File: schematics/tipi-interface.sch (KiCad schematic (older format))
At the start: 18 parts

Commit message: Update for control signalling.
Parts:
- removed R3, R?: 1k, symbol R
- removed U? (x3): 74LS21, symbol 74LS21
- removed U? (x3): 74HC04, symbol 74HC04
- removed U?: 74LS20, symbol 74LS20
- added R?: 1k, symbol R
- added U?: 74LS373, symbol 74LS373
- added U?: 74LVC245, symbol 74LVC245
- added U?: 74LS138, symbol 74LS138
- added U? (x3): 74HC04, symbol 74HC04
- added U?: 74LS21, symbol 74LS21
- added U?: 74HC245, symbol 74HC245
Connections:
- net labels removed: +5V
- wire segments 146 -> 192
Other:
- moved on the sheet: R1, U?, U?A, U?B

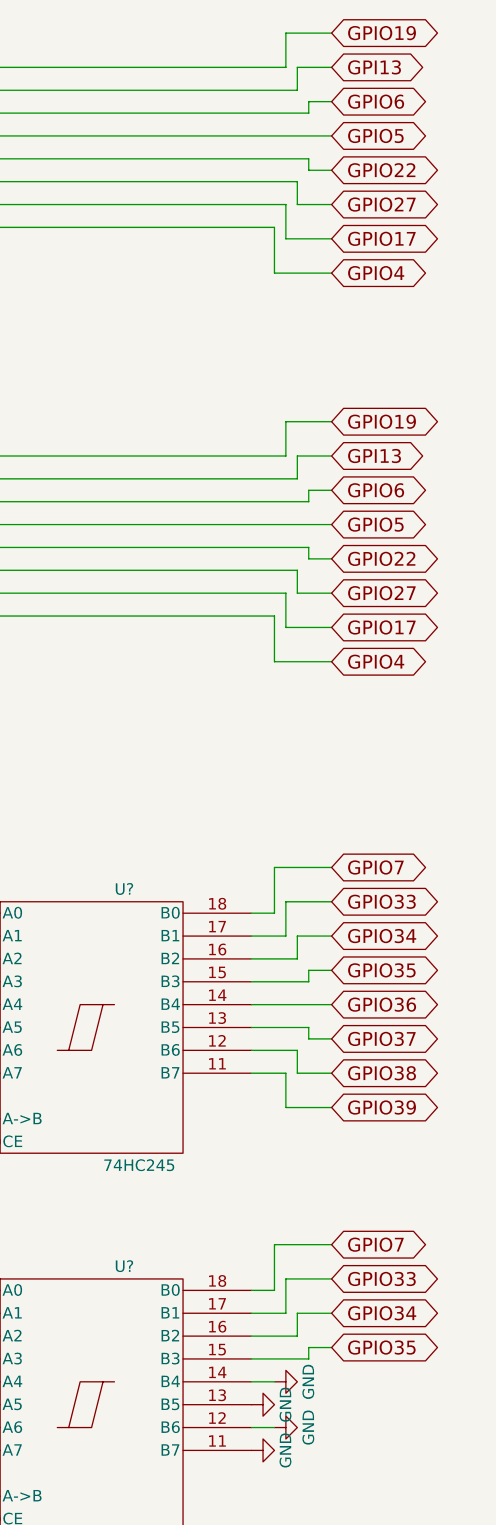
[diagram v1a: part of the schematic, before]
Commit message: Set appropriate RPi GPIO pin assignments.
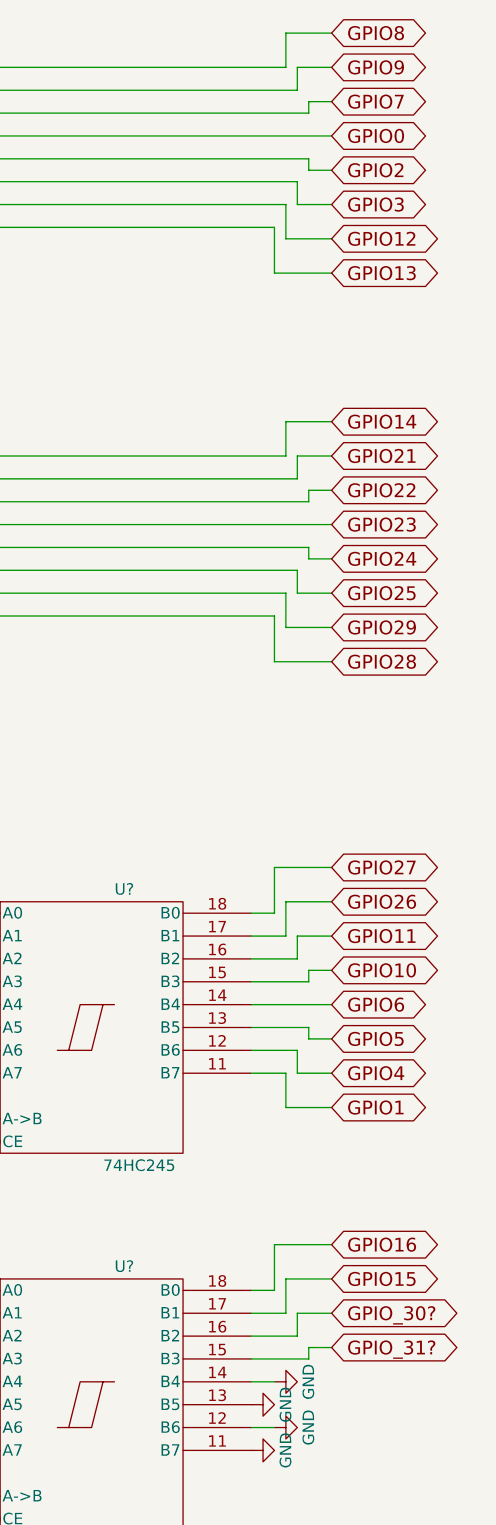
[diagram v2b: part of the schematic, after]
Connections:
- net GPIO36 is gone; now on net GPIO6: U?.14 (B4)
- net GPIO37 is gone; now on net GPIO5: U?.13 (B5)
- net GPIO38 is gone; now on net GPIO4: U?.12 (B6)
- net GPIO22: now also U?.16 (B2); no longer U?.14 (B4), U?.14 (B4)
- net GPIO27: now also U?.18 (B0); no longer U?.13 (B5), U?.13 (B5)
- net GPIO4: no longer U?.11 (B7), U?.11 (B7)
- net GPIO5: no longer U?.15 (B3), U?.15 (B3)
- net GPIO6: no longer U?.16 (B2), U?.16 (B2)
- net GPIO7: now also U?.16 (B2); no longer U?.18 (B0), U?.18 (B0)
- net GPI13 renamed GPIO21
- net GPIO21: no longer U?.17 (B1)
- net GPIO17 renamed GPIO12
- net GPIO12: no longer U?.12 (B6)
- net GPIO19 renamed GPIO14
- net GPIO14: no longer U?.18 (B0)
- net GPIO33 renamed GPIO15
- net GPIO15: no longer U?.17 (B1)
- net GPIO34 renamed GPIO11
- net GPIO11: no longer U?.16 (B2)
- net GPIO35 renamed GPIO10
- net GPIO10: no longer U?.15 (B3)
- net GPIO39 renamed GPIO1
- new net GPIO0: U?.15 (B3)
- new net GPIO13: U?.11 (B7)
- new net GPIO16: U?.18 (B0)
- new net GPIO2: U?.14 (B4)
- new net GPIO23: U?.15 (B3)
- new net GPIO24: U?.14 (B4)
- new net GPIO25: U?.13 (B5)
- new net GPIO26: U?.17 (B1)
- new net GPIO28: U?.11 (B7)
- new net GPIO29: U?.12 (B6)
- new net GPIO3: U?.13 (B5)
- new net GPIO8: U?.18 (B0)
- new net GPIO9: U?.17 (B1)
- new net GPIO_30?: U?.16 (B2)
- new net GPIO_31?: U?.15 (B3)
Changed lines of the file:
@@
 $EndComp
 Text GLabel 10050 3150 2    60   BiDi ~ 0
-GPIO19
+GPIO14
 Text GLabel 10050 3300 2    60   BiDi ~ 0
-GPI13
+GPIO21
 Text GLabel 10050 3450 2    60   BiDi ~ 0
-GPIO6
+GPIO22
 Text GLabel 10050 3600 2    60   BiDi ~ 0
-GPIO5
+GPIO23
 Text GLabel 10050 3750 2    60   BiDi ~ 0
-GPIO22
+GPIO24
 Text GLabel 10050 3900 2    60   BiDi ~ 0
-GPIO27
+GPIO25
 Text GLabel 10050 4050 2    60   BiDi ~ 0
-GPIO17
+GPIO29
 Text GLabel 10050 4200 2    60   BiDi ~ 0
-GPIO4
+GPIO28
 $Comp
 L 74LS373 U?
@@
 $EndComp
 Text GLabel 10050 5100 2    60   BiDi ~ 0
-GPIO7
+GPIO27
 Text GLabel 10050 5250 2    60   BiDi ~ 0
-GPIO33
+GPIO26
 Text GLabel 10050 5400 2    60   BiDi ~ 0
-GPIO34
+GPIO11
 Text GLabel 10050 5550 2    60   BiDi ~ 0
-GPIO35
+GPIO10
 Text GLabel 10050 5700 2    60   BiDi ~ 0
-GPIO36
+GPIO6
 Text GLabel 10050 5850 2    60   BiDi ~ 0
-GPIO37
+GPIO5
 Text GLabel 10050 6000 2    60   BiDi ~ 0
-GPIO38
+GPIO4
 Text GLabel 10050 6150 2    60   BiDi ~ 0
-GPIO39
+GPIO1
 Entry Wire Line
 	8200 5200 8300 5300
@@
 $EndComp
 Text GLabel 10050 1450 2    60   BiDi ~ 0
-GPIO19
+GPIO8
 Text GLabel 10050 1600 2    60   BiDi ~ 0
-GPI13
+GPIO9
 Text GLabel 10050 1750 2    60   BiDi ~ 0
-GPIO6
+GPIO7
 Text GLabel 10050 1900 2    60   BiDi ~ 0
-GPIO5
+GPIO0
 Text GLabel 10050 2050 2    60   BiDi ~ 0
-GPIO22
+GPIO2
 Text GLabel 10050 2200 2    60   BiDi ~ 0
-GPIO27
+GPIO3
 Text GLabel 10050 2350 2    60   BiDi ~ 0
-GPIO17
+GPIO12
 Text GLabel 10050 2500 2    60   BiDi ~ 0
-GPIO4
+GPIO13
 $Comp
 L 74LS373 U?
@@
 $EndComp
 Text GLabel 10050 6750 2    60   BiDi ~ 0
-GPIO7
+GPIO16
 Text GLabel 10050 6900 2    60   BiDi ~ 0
-GPIO33
+GPIO15
 Text GLabel 10050 7050 2    60   BiDi ~ 0
-GPIO34
+GPIO_30?
 Text GLabel 10050 7200 2    60   BiDi ~ 0
-GPIO35
-$Comp
-L GND #PWR?
+GPIO_31?
+$Comp
+L GND #PWR?

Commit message: Add CRU bit to enable/disable board.
Use a 4 bit jumper header block to select nibble x in the address 1x00h. The bit responds at any and all addresses inclusively between 1x00h and 1xFFh. However the circuit should be programmed to bit offset 0 only. Future bits
will be intendend for bank switch ROM.
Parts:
- added P?: CONN_02X04, symbol CONN_02X04
- added R? (x5): 1k, symbol R
- added U?: 74LS688, symbol 74LS688
- added U?: 74LS74, symbol 74LS74
- added U?: 7402, symbol 7402
- added U?: 74LS08, symbol 74LS08
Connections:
- net labels added: +5V, CRU-BIT1, RESET*
- wire segments 192 -> 234
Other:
- moved on the sheet: R1, R?, U?, U?A, U?B

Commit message: Fix issue with cru addressing off by a bit.
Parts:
- removed P?: CONN_02X04, symbol CONN_02X04
- added R?: 1k, symbol R
- added SW?: Coded_Switch, symbol Coded_Switch
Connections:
- wire segments 234 -> 231
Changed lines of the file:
@@
 Sheet 1 1
 Title "TI Raspberry PI interface"
-Date "2017-01-21"
+Date "2017-01-22"
 Rev "4"
 Comp "ElectricLab & Jedimatt42"
@@
 L GND #PWR?
 U 1 1 5882E6A1
-P 2000 1150
-F 0 "#PWR?" H 2000 900 50  0001 C CNN
-F 1 "GND" H 2000 1000 50  0000 C CNN
-F 2 "" H 2000 1150 50  0000 C CNN
-F 3 "" H 2000 1150 50  0000 C CNN
-	1    2000 1150
+P 2000 1450
+F 0 "#PWR?" H 2000 1200 50  0001 C CNN
+F 1 "GND" H 2000 1300 50  0000 C CNN
+F 2 "" H 2000 1450 50  0000 C CNN
+F 3 "" H 2000 1450 50  0000 C CNN
+	1    2000 1450
 	0    1    1    0
-$EndComp
-$Comp
-L CONN_02X04 P?
-U 1 1 5882E705
-P 1250 1750
-F 0 "P?" H 1250 2000 50  0000 C CNN
-F 1 "CONN_02X04" H 1250 1500 50  0000 C CNN
-F 2 "" H 1250 550 50  0000 C CNN
-F 3 "" H 1250 550 50  0000 C CNN
-	1    1250 1750
-	1    0    0    -1
 $EndComp
 $Comp
@@
 $Comp
 L GND #PWR?
-U 1 1 588304B3
-P 900 1900
-F 0 "#PWR?" H 900 1650 50  0001 C CNN
-F 1 "GND" H 900 1750 50  0000 C CNN
-F 2 "" H 900 1900 50  0000 C CNN
-F 3 "" H 900 1900 50  0000 C CNN
-	1    900  1900
-	1    0    0    -1
-$EndComp
-$Comp
-L GND #PWR?
 U 1 1 5883155D
-P 2050 2000
-F 0 "#PWR?" H 2050 1750 50  0001 C CNN
-F 1 "GND" H 2050 1850 50  0000 C CNN
-F 2 "" H 2050 2000 50  0000 C CNN
-F 3 "" H 2050 2000 50  0000 C CNN
-	1    2050 2000
+P 2050 2300
+F 0 "#PWR?" H 2050 2050 50  0001 C CNN
+F 1 "GND" H 2050 2150 50  0000 C CNN
+F 2 "" H 2050 2300 50  0000 C CNN
+F 3 "" H 2050 2300 50  0000 C CNN
+	1    2050 2300
 	0    1    1    0
 $EndComp
@@
 	7650 9100 8250 9100
 Wire Wire Line
-	900  1600 1000 1600
-Wire Wire Line
-	900  1600 900  1900
-Wire Wire Line
-	900  1700 1000 1700
-Wire Wire Line
-	900  1800 1000 1800
-Connection ~ 900  1700
-Wire Wire Line
-	900  1900 1000 1900
-Connection ~ 900  1800
-Wire Wire Line
 	1500 1600 2100 1600
 Wire Wire Line
@@
 	1500 1900 2100 1900
 Wire Wire Line
-	2050 2000 2100 2000
-Wire Wire Line
-	2050 2000 2050 2450
+	1800 2000 2100 2000
+Wire Wire Line
+	2050 2100 2050 2450
 Wire Wire Line
 	2050 2300 2100 2300
@@
 Wire Wire Line
 	2100 2100 2050 2100
-Connection ~ 2050 2100
 Wire Wire Line
 	2050 2450 2100 2450
@@
 	1250 2300 1200 2300
 Connection ~ 1200 2300
-Connection ~ 900  1900
-Wire Wire Line
-	1200 2150 1200 2600
+Wire Wire Line
+	1200 2150 1200 2750
 Wire Wire Line
 	1200 2600 1350 2600
 Connection ~ 1200 2600
 Wire Wire Line
-	2100 1150 2000 1150
+	1550 1150 2100 1150
 Wire Wire Line
 	2100 1250 2000 1250
-Wire Wire Line
-	2000 1150 2000 1450
-Wire Wire Line
-	2000 1350 2100 1350
-Connection ~ 2000 1250
 Wire Wire Line
 	2000 1450 2100 1450
 Connection ~ 2000 1350
 Text GLabel 1750 1050 0    60   Input ~ 0
-A3
+A4
 Text GLabel 1550 950  0    60   Input ~ 0
-A4
+A5
 Text GLabel 1750 850  0    60   Input ~ 0
-A5
+A6
 Text GLabel 1550 750  0    60   Input ~ 0
-A6
+A7
 Wire Wire Line
 	1750 1050 2100 1050
@@
 Wire Wire Line
 	2000 6550 2100 6550
+$Comp
+L R R?
+U 1 1 5884EBE6
+P 1800 2150
+F 0 "R?" V 1880 2150 50  0000 C CNN
+F 1 "1k" V 1800 2150 50  0000 C CNN
+F 2 "" V 1730 2150 50  0000 C CNN
+F 3 "" H 1800 2150 50  0000 C CNN
+	1    1800 2150
+	-1   0    0    1
+$EndComp
+Wire Wire Line
+	1800 2300 1800 2750
+Wire Wire Line
+	1800 2750 1200 2750
+Wire Wire Line
+	2000 1250 2000 1450
+Text GLabel 1550 1150 0    60   Input ~ 0
+A3
+$Comp
+L Coded_Switch SW?
+U 1 1 5884F44E
+P 900 1650
+F 0 "SW?" H 1000 2000 50  0000 C CNN
+F 1 "Coded_Switch" H 900 1301 50  0000 C CNN
+F 2 "" H 900 1650 50  0000 C CNN
+F 3 "" H 900 1650 50  0000 C CNN
+	1    900  1650
+	1    0    0    -1
+$EndComp
+Wire Wire Line
+	2000 1350 2100 1350
+$Comp
+L GND #PWR?
+U 1 1 5884F7D2
+P 1500 1400
+F 0 "#PWR?" H 1500 1150 50  0001 C CNN
+F 1 "GND" H 1500 1250 50  0000 C CNN
+F 2 "" H 1500 1400 50  0000 C CNN
+F 3 "" H 1500 1400 50  0000 C CNN
+	1    1500 1400
+	0    -1   -1   0
+$EndComp
 $EndSCHEMATC

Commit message: Tweaked pin assignements in schematic for interface.
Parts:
- U? (x4): symbol 74LS21 -> 74LS21-RESCUE-tipi-interface
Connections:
- net GPIO_30? is gone; now on net GPIO1: U?.16 (B2)
- net GPIO_31? is gone; now on net GND: U?.15 (B3)
- net GND: now also U?.11 (B7)
- net GPIO1: no longer U?.11 (B7)
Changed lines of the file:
@@
 EESchema Schematic File Version 2
+LIBS:tipi-interface-rescue
 LIBS:power
 LIBS:device
@@
 	4950 5050 5050 5150
 $Comp
-L 74LS21 U?
+L 74LS21-RESCUE-tipi-interface U?
 U 2 1 5872ED3F
 P 3350 8200
@@
 $EndComp
 $Comp
-L 74LS21 U?
+L 74LS21-RESCUE-tipi-interface U?
 U 1 1 5872EDA9
 P 3350 8800
@@
 $EndComp
 $Comp
-L 74LS21 U?
+L 74LS21-RESCUE-tipi-interface U?
 U 2 1 5872EDEA
 P 3350 9400
@@
 Text GLabel 10000 7150 2    60   BiDi ~ 0
 GPIO4
-Text GLabel 10000 7300 2    60   BiDi ~ 0
+Text GLabel 9850 8300 2    60   BiDi ~ 0
 GPIO1
 Entry Wire Line
@@
 $EndComp
 $Comp
-L 74LS21 U?
+L 74LS21-RESCUE-tipi-interface U?
 U 1 1 587EEED4
 P 4800 8250
@@
 Text GLabel 10000 8050 2    60   BiDi ~ 0
 GPIO15
-Text GLabel 10000 8200 2    60   BiDi ~ 0
-GPIO_30?
-Text GLabel 10000 8350 2    60   BiDi ~ 0
-GPIO_31?
 $Comp
 L GND #PWR?
@@
 Wire Wire Line
 	4450 3650 5050 3650
-Wire Wire Line
-	9650 8400 9900 8400
-Wire Wire Line
-	9900 8400 9900 8350
-Wire Wire Line
-	9900 8350 10000 8350
-Wire Wire Line
-	9650 8300 9850 8300
-Wire Wire Line
-	9850 8300 9850 8200
-Wire Wire Line
-	9850 8200 10000 8200
 Wire Wire Line
 	9650 8200 9800 8200
@@
 	0    -1   -1   0
 $EndComp
+$Comp
+L GND #PWR?
+U 1 1 58857196
+P 9650 8400
+F 0 "#PWR?" H 9650 8150 50  0001 C CNN
+F 1 "GND" H 9650 8250 50  0000 C CNN
+F 2 "" H 9650 8400 50  0000 C CNN
+F 3 "" H 9650 8400 50  0000 C CNN
+	1    9650 8400
+	0    -1   -1   0
+$EndComp
+$Comp
+L GND #PWR?
+U 1 1 588571F8
+P 10000 7300
+F 0 "#PWR?" H 10000 7050 50  0001 C CNN
+F 1 "GND" H 10000 7150 50  0000 C CNN
+F 2 "" H 10000 7300 50  0000 C CNN
+F 3 "" H 10000 7300 50  0000 C CNN
+	1    10000 7300
+	0    -1   -1   0
+$EndComp
+Wire Wire Line
+	9650 8300 9850 8300
 $EndSCHEMATC

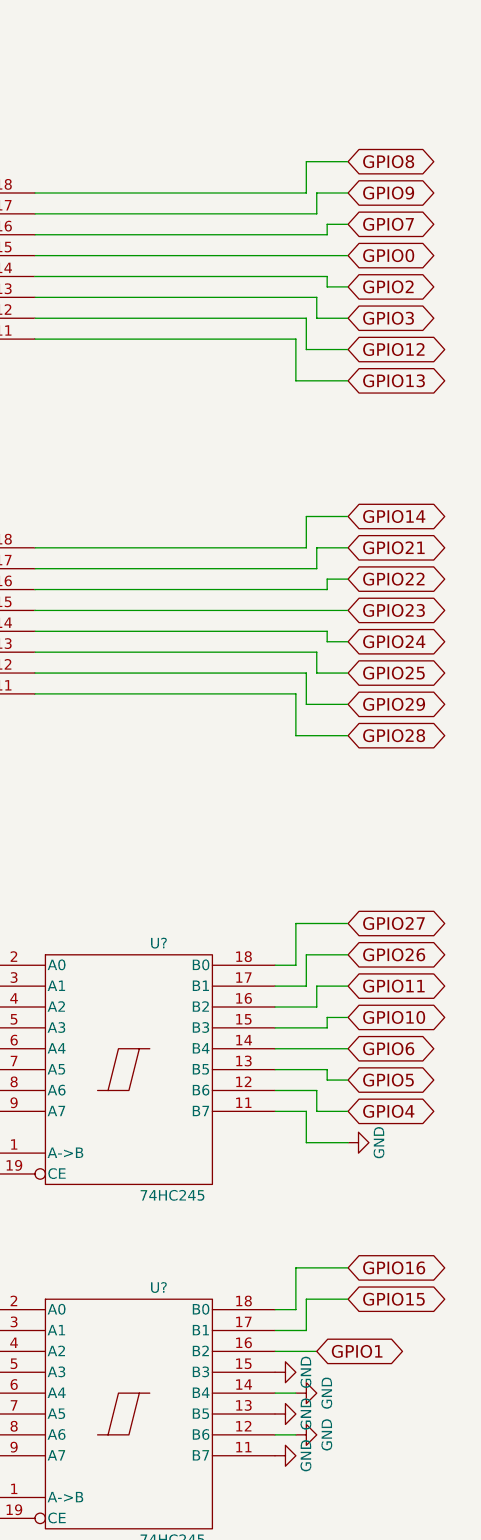
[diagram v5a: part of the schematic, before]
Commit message: Update drawing with Raspberry PI pin assignments.
See table in schematics/rpi-pinouts. BCM numbers are used to label in schematic.
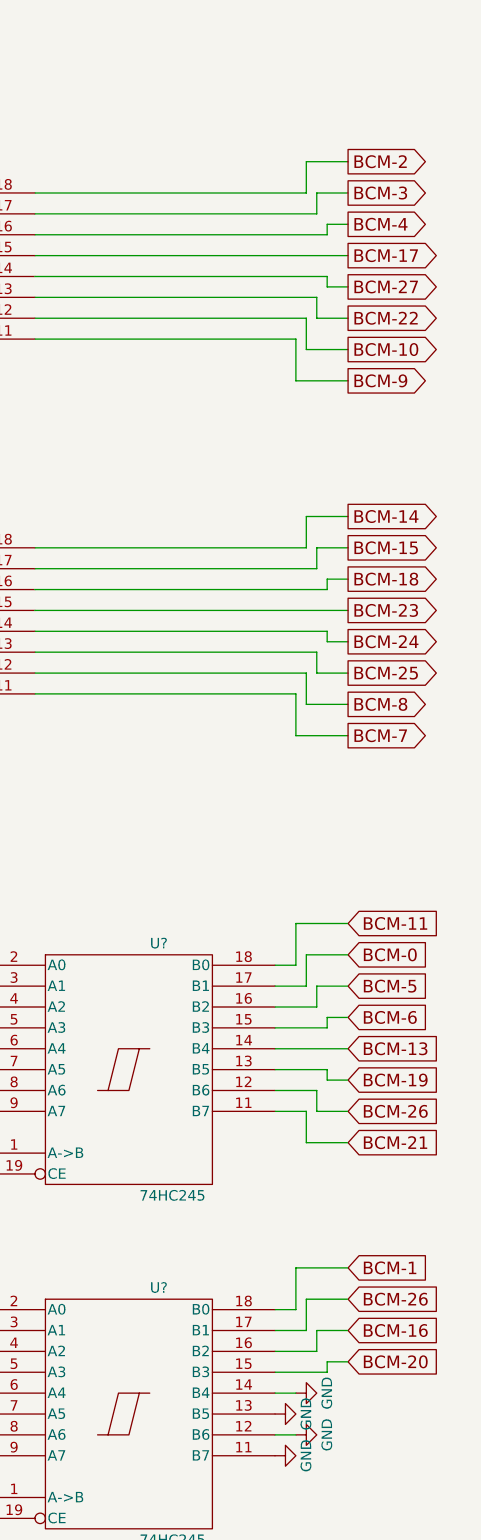
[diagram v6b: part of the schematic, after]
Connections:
- net GPIO4 is gone; now on net BCM-26: U?.12 (B6)
- net GND: no longer U?.11 (B7), U?.15 (B3)
- net GPIO0 renamed BCM-17
- net GPIO1 renamed BCM-16
- net GPIO10 renamed BCM-6
- net GPIO11 renamed BCM-5
- net GPIO12 renamed BCM-10
- net GPIO13 renamed BCM-9
- net GPIO14 renamed BCM-14
- net GPIO15 renamed BCM-26
- net GPIO16 renamed BCM-1
- net GPIO2 renamed BCM-27
- net GPIO21 renamed BCM-15
- net GPIO22 renamed BCM-18
- net GPIO23 renamed BCM-23
- net GPIO24 renamed BCM-24
- net GPIO25 renamed BCM-25
- net GPIO26 renamed BCM-0
- net GPIO27 renamed BCM-11
- net GPIO28 renamed BCM-7
- net GPIO29 renamed BCM-8
- net GPIO3 renamed BCM-22
- net GPIO5 renamed BCM-19
- net GPIO6 renamed BCM-13
- net GPIO7 renamed BCM-4
- net GPIO8 renamed BCM-2
- net GPIO9 renamed BCM-3
- new net BCM-20: U?.15 (B3)
- new net BCM-21: U?.11 (B7)
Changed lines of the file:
@@
 EESchema Schematic File Version 2
-LIBS:tipi-interface-rescue
 LIBS:power
 LIBS:device
@@
 	1    0    0    -1
 $EndComp
-Text GLabel 10000 4300 2    60   BiDi ~ 0
-GPIO14
-Text GLabel 10000 4450 2    60   BiDi ~ 0
-GPIO21
-Text GLabel 10000 4600 2    60   BiDi ~ 0
-GPIO22
-Text GLabel 10000 4750 2    60   BiDi ~ 0
-GPIO23
-Text GLabel 10000 4900 2    60   BiDi ~ 0
-GPIO24
-Text GLabel 10000 5050 2    60   BiDi ~ 0
-GPIO25
-Text GLabel 10000 5200 2    60   BiDi ~ 0
-GPIO29
-Text GLabel 10000 5350 2    60   BiDi ~ 0
-GPIO28
+Text GLabel 10000 4300 2    60   Output ~ 0
+BCM-14
+Text GLabel 10000 4450 2    60   Output ~ 0
+BCM-15
+Text GLabel 10000 4600 2    60   Output ~ 0
+BCM-18
+Text GLabel 10000 4750 2    60   Output ~ 0
+BCM-23
+Text GLabel 10000 4900 2    60   Output ~ 0
+BCM-24
+Text GLabel 10000 5050 2    60   Output ~ 0
+BCM-25
+Text GLabel 10000 5200 2    60   Output ~ 0
+BCM-8
+Text GLabel 10000 5350 2    60   Output ~ 0
+BCM-7
 $Comp
 L 74LS373 U?
@@
 	1    0    0    -1
 $EndComp
-Text GLabel 10000 6250 2    60   BiDi ~ 0
-GPIO27
-Text GLabel 10000 6400 2    60   BiDi ~ 0
-GPIO26
-Text GLabel 10000 6550 2    60   BiDi ~ 0
-GPIO11
-Text GLabel 10000 6700 2    60   BiDi ~ 0
-GPIO10
-Text GLabel 10000 6850 2    60   BiDi ~ 0
-GPIO6
-Text GLabel 10000 7000 2    60   BiDi ~ 0
-GPIO5
-Text GLabel 10000 7150 2    60   BiDi ~ 0
-GPIO4
-Text GLabel 9850 8300 2    60   BiDi ~ 0
-GPIO1
+Text GLabel 10000 6250 2    60   Input ~ 0
+BCM-11
+Text GLabel 10000 6400 2    60   Input ~ 0
+BCM-0
+Text GLabel 10000 6550 2    60   Input ~ 0
+BCM-5
+Text GLabel 10000 6700 2    60   Input ~ 0
+BCM-6
+Text GLabel 10000 6850 2    60   Input ~ 0
+BCM-13
+Text GLabel 10000 7000 2    60   Input ~ 0
+BCM-19
+Text GLabel 10000 7150 2    60   Input ~ 0
+BCM-26
+Text GLabel 10000 8200 2    60   Input ~ 0
+BCM-16
 Entry Wire Line
 	8150 6350 8250 6450
@@
 	1    0    0    -1
 $EndComp
-Text GLabel 10000 2600 2    60   BiDi ~ 0
-GPIO8
-Text GLabel 10000 2750 2    60   BiDi ~ 0
-GPIO9
-Text GLabel 10000 2900 2    60   BiDi ~ 0
-GPIO7
-Text GLabel 10000 3050 2    60   BiDi ~ 0
-GPIO0
-Text GLabel 10000 3200 2    60   BiDi ~ 0
-GPIO2
-Text GLabel 10000 3350 2    60   BiDi ~ 0
-GPIO3
-Text GLabel 10000 3500 2    60   BiDi ~ 0
-GPIO12
-Text GLabel 10000 3650 2    60   BiDi ~ 0
-GPIO13
+Text GLabel 10000 2600 2    60   Output ~ 0
+BCM-2
+Text GLabel 10000 2750 2    60   Output ~ 0
+BCM-3
+Text GLabel 10000 2900 2    60   Output ~ 0
+BCM-4
+Text GLabel 10000 3050 2    60   Output ~ 0
+BCM-17
+Text GLabel 10000 3200 2    60   Output ~ 0
+BCM-27
+Text GLabel 10000 3350 2    60   Output ~ 0
+BCM-22
+Text GLabel 10000 3500 2    60   Output ~ 0
+BCM-10
+Text GLabel 10000 3650 2    60   Output ~ 0
+BCM-9
 $Comp
 L 74LS373 U?
@@
 	1    0    0    -1
 $EndComp
-Text GLabel 10000 7900 2    60   BiDi ~ 0
-GPIO16
-Text GLabel 10000 8050 2    60   BiDi ~ 0
-GPIO15
+Text GLabel 10000 7900 2    60   Input ~ 0
+BCM-1
+Text GLabel 10000 8050 2    60   Input ~ 0
+BCM-26
 $Comp
 L GND #PWR?
@@
 	0    -1   -1   0
 $EndComp
-$Comp
-L GND #PWR?
-U 1 1 58857196
-P 9650 8400
-F 0 "#PWR?" H 9650 8150 50  0001 C CNN
-F 1 "GND" H 9650 8250 50  0000 C CNN
-F 2 "" H 9650 8400 50  0000 C CNN
-F 3 "" H 9650 8400 50  0000 C CNN
-	1    9650 8400
-	0    -1   -1   0
-$EndComp
-$Comp
-L GND #PWR?
-U 1 1 588571F8
-P 10000 7300
-F 0 "#PWR?" H 10000 7050 50  0001 C CNN
-F 1 "GND" H 10000 7150 50  0000 C CNN
-F 2 "" H 10000 7300 50  0000 C CNN
-F 3 "" H 10000 7300 50  0000 C CNN
-	1    10000 7300
-	0    -1   -1   0
-$EndComp
 Wire Wire Line
 	9650 8300 9850 8300
+Text GLabel 10000 8350 2    60   Input ~ 0
+BCM-20
+Wire Wire Line
+	9850 8300 9850 8200
+Wire Wire Line
+	9850 8200 10000 8200
+Wire Wire Line
+	9650 8400 9900 8400
+Wire Wire Line
+	9900 8400 9900 8350
+Wire Wire Line
+	9900 8350 10000 8350
+Text GLabel 10000 7300 2    60   Input ~ 0
+BCM-21
 $EndSCHEMATC
